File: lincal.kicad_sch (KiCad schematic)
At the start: 0 parts

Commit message: Most blocks there....
About to restore scan.
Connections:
- no-connect marks 2 -> 6
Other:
- sheet DAC2752-1A ports: added none; removed Comp
- sheet DAC2752-1B ports: added none; removed Comp
- sheet DAC2752-2A ports: added none; removed Comp
- sheet DAC2752-2B ports: added none; removed Comp
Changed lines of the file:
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@@
 	(paper "A4")
 	(no_connect
+		(at 195.58 110.49)
+	)
+	(no_connect
+		(at 195.58 120.65)
+	)
+	(no_connect
 		(at 195.58 118.11)
+	)
+	(no_connect
+		(at 195.58 107.95)
+	)
+	(no_connect
+		(at 195.58 113.03)
 	)
 	(no_connect
@@
 	(wire
 		(pts
+			(xy 194.31 120.65) (xy 195.58 120.65)
+		)
+		(stroke
+			(width 0)
+			(type default)
+		)
+	)
+	(wire
+		(pts
 			(xy 48.26 142.24) (xy 58.42 142.24)
 		)
@@
 	(wire
 		(pts
+			(xy 194.31 113.03) (xy 195.58 113.03)
+		)
+		(stroke
+			(width 0)
+			(type default)
+		)
+	)
+	(wire
+		(pts
 			(xy 58.42 146.05) (xy 48.26 146.05)
 		)
@@
 	(wire
 		(pts
+			(xy 194.31 110.49) (xy 195.58 110.49)
+		)
+		(stroke
+			(width 0)
+			(type default)
+		)
+	)
+	(wire
+		(pts
 			(xy 176.53 102.87) (xy 167.64 102.87)
 		)
@@
 	(wire
 		(pts
-			(xy 194.31 110.49) (xy 204.47 110.49)
-		)
-		(stroke
-			(width 0)
-			(type default)
-		)
-	)
-	(wire
-		(pts
-			(xy 194.31 113.03) (xy 204.47 113.03)
+			(xy 194.31 102.87) (xy 204.47 102.87)
 		)
 		(stroke
@@
 	(wire
 		(pts
-			(xy 194.31 107.95) (xy 204.47 107.95)
-		)
-		(stroke
-			(width 0)
-			(type default)
-		)
-	)
-	(wire
-		(pts
 			(xy 81.28 148.59) (xy 90.17 148.59)
 		)
@@
 	(wire
 		(pts
-			(xy 194.31 120.65) (xy 204.47 120.65)
+			(xy 194.31 105.41) (xy 204.47 105.41)
 		)
 		(stroke
@@
 	(wire
 		(pts
-			(xy 58.42 78.74) (xy 48.26 78.74)
-		)
-		(stroke
-			(width 0)
-			(type default)
-		)
-	)
-	(wire
-		(pts
 			(xy 140.97 57.15) (xy 148.59 57.15)
 		)
@@
 	(wire
 		(pts
-			(xy 58.42 116.84) (xy 48.26 116.84)
-		)
-		(stroke
-			(width 0)
-			(type default)
-		)
-	)
-	(wire
-		(pts
 			(xy 198.12 77.47) (xy 207.01 77.47)
 		)
@@
 	(wire
 		(pts
-			(xy 194.31 102.87) (xy 204.47 102.87)
-		)
-		(stroke
-			(width 0)
-			(type default)
-		)
-	)
-	(wire
-		(pts
 			(xy 198.12 59.69) (xy 207.01 59.69)
 		)
@@
 	(wire
 		(pts
-			(xy 58.42 104.14) (xy 48.26 104.14)
-		)
-		(stroke
-			(width 0)
-			(type default)
-		)
-	)
-	(wire
-		(pts
-			(xy 58.42 91.44) (xy 48.26 91.44)
+			(xy 194.31 107.95) (xy 195.58 107.95)
 		)
 		(stroke
@@
 		(pts
 			(xy 114.3 57.15) (xy 105.41 57.15)
-		)
-		(stroke
-			(width 0)
-			(type default)
-		)
-	)
-	(wire
-		(pts
-			(xy 194.31 105.41) (xy 204.47 105.41)
 		)
 		(stroke
@@
 		)
 	)
-	(label "Comp2A"
-		(at 48.26 104.14 0)
-		(effects
-			(font
-				(size 1.27 1.27)
-			)
-			(justify left bottom)
-		)
-	)
 	(label "MonB1"
 		(at 90.17 148.59 180)
@@
 		)
 	)
-	(label "Comp2A"
-		(at 204.47 107.95 180)
-		(effects
-			(font
-				(size 1.27 1.27)
-			)
-			(justify right bottom)
-		)
-	)
 	(label "~{CSDAC1}"
 		(at 90.17 57.15 180)
@@
 	)
 	(label "MonTC"
-		(at 204.47 113.03 180)
+		(at 204.47 102.87 180)
 		(effects
 			(font
@@
 	)
 	(label "Ref2V16"
-		(at 204.47 120.65 180)
-		(effects
-			(font
-				(size 1.27 1.27)
-			)
-			(justify right bottom)
-		)
-	)
-	(label "Comp2B"
-		(at 48.26 116.84 0)
-		(effects
-			(font
-				(size 1.27 1.27)
-			)
-			(justify left bottom)
-		)
-	)
-	(label "Comp1A"
-		(at 48.26 78.74 0)
-		(effects
-			(font
-				(size 1.27 1.27)
-			)
-			(justify left bottom)
+		(at 204.47 105.41 180)
+		(effects
+			(font
+				(size 1.27 1.27)
+			)
+			(justify right bottom)
 		)
 	)
@@
 		)
 	)
-	(label "Comp2B"
-		(at 204.47 110.49 180)
-		(effects
-			(font
-				(size 1.27 1.27)
-			)
-			(justify right bottom)
-		)
-	)
 	(label "OffsetA2"
 		(at 207.01 62.23 180)
@@
 		)
 	)
-	(label "Comp1B"
-		(at 48.26 91.44 0)
-		(effects
-			(font
-				(size 1.27 1.27)
-			)
-			(justify left bottom)
-		)
-	)
 	(label "Sel1A"
 		(at 162.56 72.39 0)
@@
 		)
 	)
-	(label "Comp1B"
-		(at 204.47 105.41 180)
-		(effects
-			(font
-				(size 1.27 1.27)
-			)
-			(justify right bottom)
-		)
-	)
 	(label "MOSI"
 		(at 49.53 57.15 0)
@@
 			)
 			(justify left bottom)
-		)
-	)
-	(label "Comp1A"
-		(at 204.47 102.87 180)
-		(effects
-			(font
-				(size 1.27 1.27)
-			)
-			(justify right bottom)
 		)
 	)
@@
 			)
 		)
-		(pin "Comp" input
-			(at 58.42 91.44 180)
-			(effects
-				(font
-					(size 1.27 1.27)
-				)
-				(justify left)
-			)
-		)
 		(pin "Select" input
 			(at 81.28 90.17 0)
@@
 			)
 		)
-		(pin "Comp" input
-			(at 58.42 104.14 180)
-			(effects
-				(font
-					(size 1.27 1.27)
-				)
-				(justify left)
-			)
-		)
 		(pin "Select" input
 			(at 81.28 102.87 0)
@@
 			)
 		)
-		(pin "Comp" input
-			(at 58.42 116.84 180)
-			(effects
-				(font
-					(size 1.27 1.27)
-				)
-				(justify left)
-			)
-		)
 		(pin "Select" input
 			(at 81.28 115.57 0)
@@
 			(effects
 				(font
-					(size 1.27 1.27)
-				)
-				(justify left)
-			)
-		)
-		(pin "Comp" input
-			(at 58.42 78.74 180)
-			(effects
-				(font

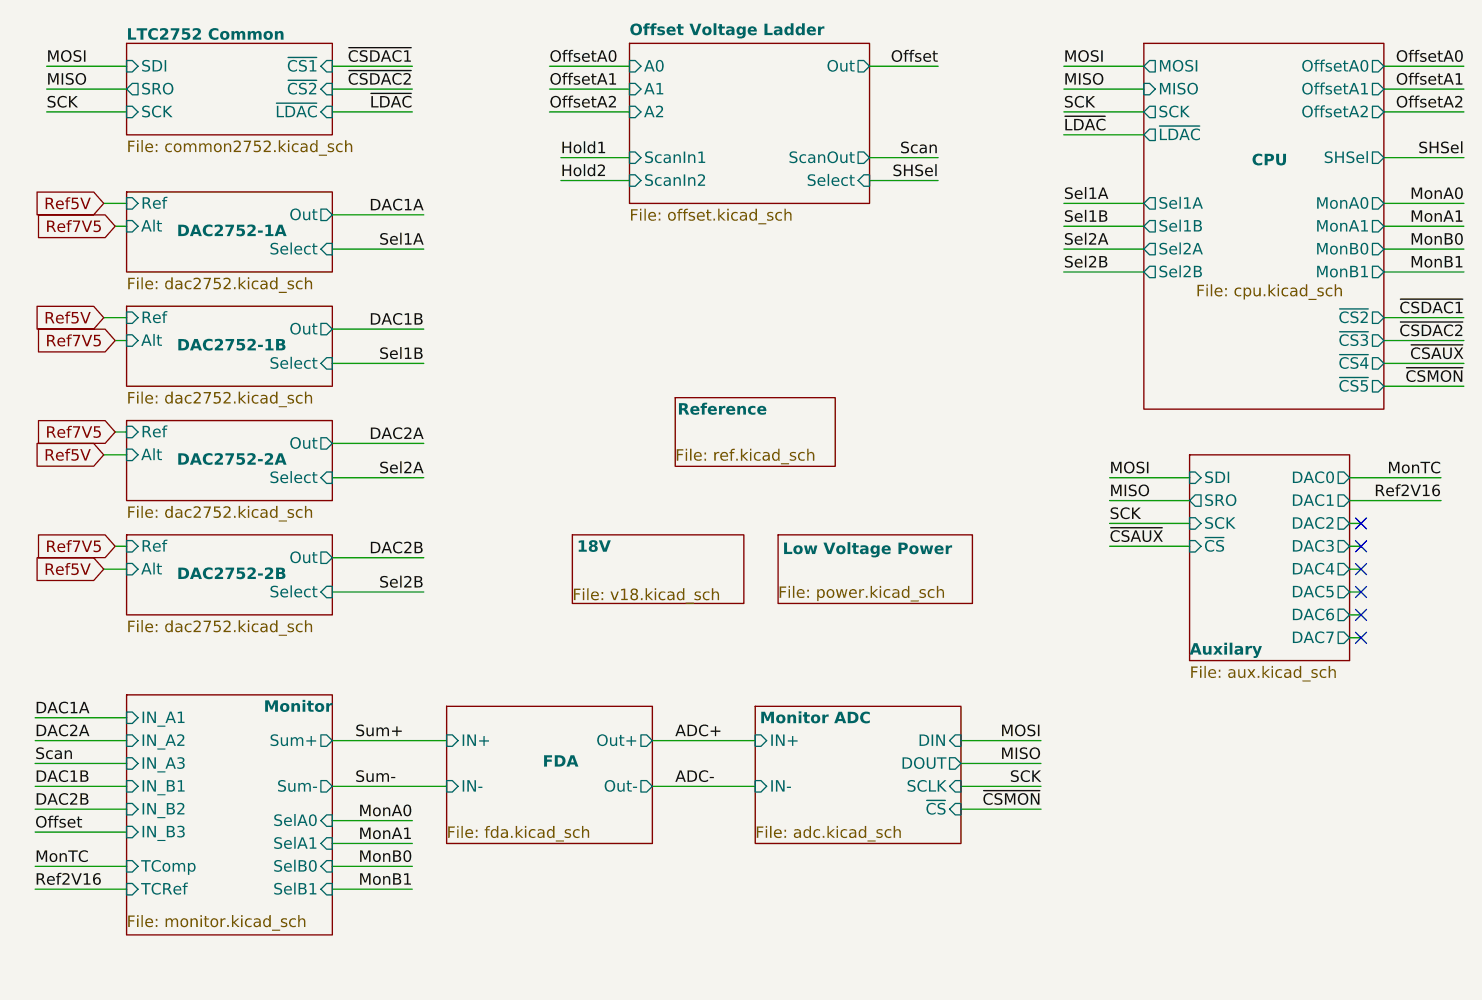
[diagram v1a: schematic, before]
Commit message: S&H restored.  Now to touch up connections etc.
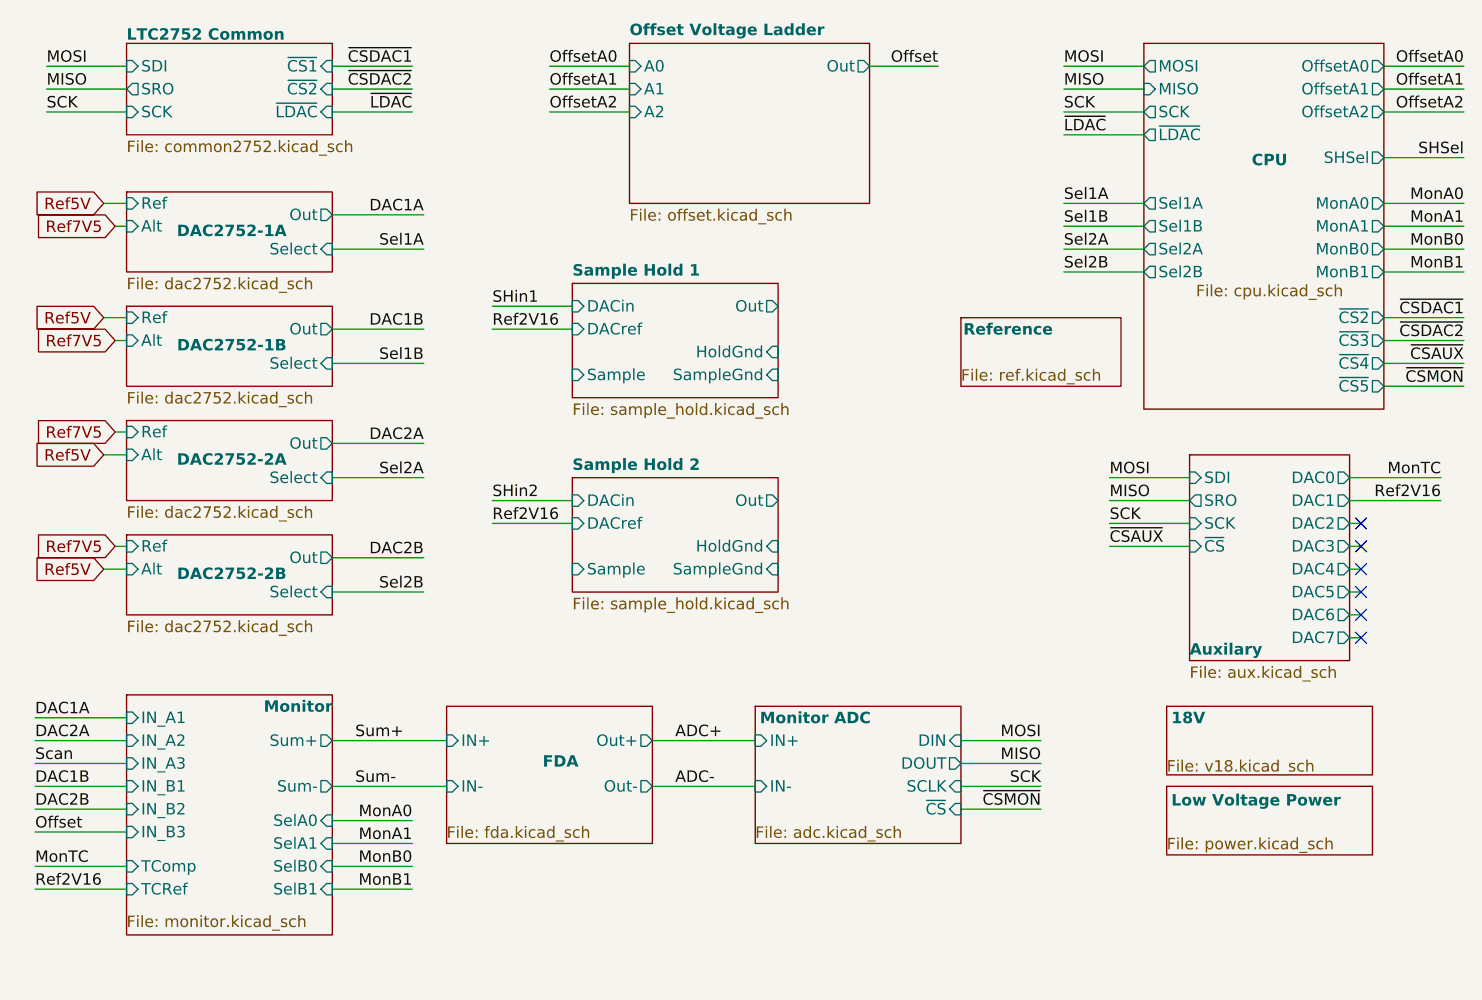
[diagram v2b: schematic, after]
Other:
- added sheet Sample Hold 1 (sample_hold.kicad_sch)
- added sheet Sample Hold 2 (sample_hold.kicad_sch)
- sheet Offset Voltage Ladder ports: added none; removed ScanIn1, ScanIn2, ScanOut, Select

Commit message: Put ref filtering into the schematic.
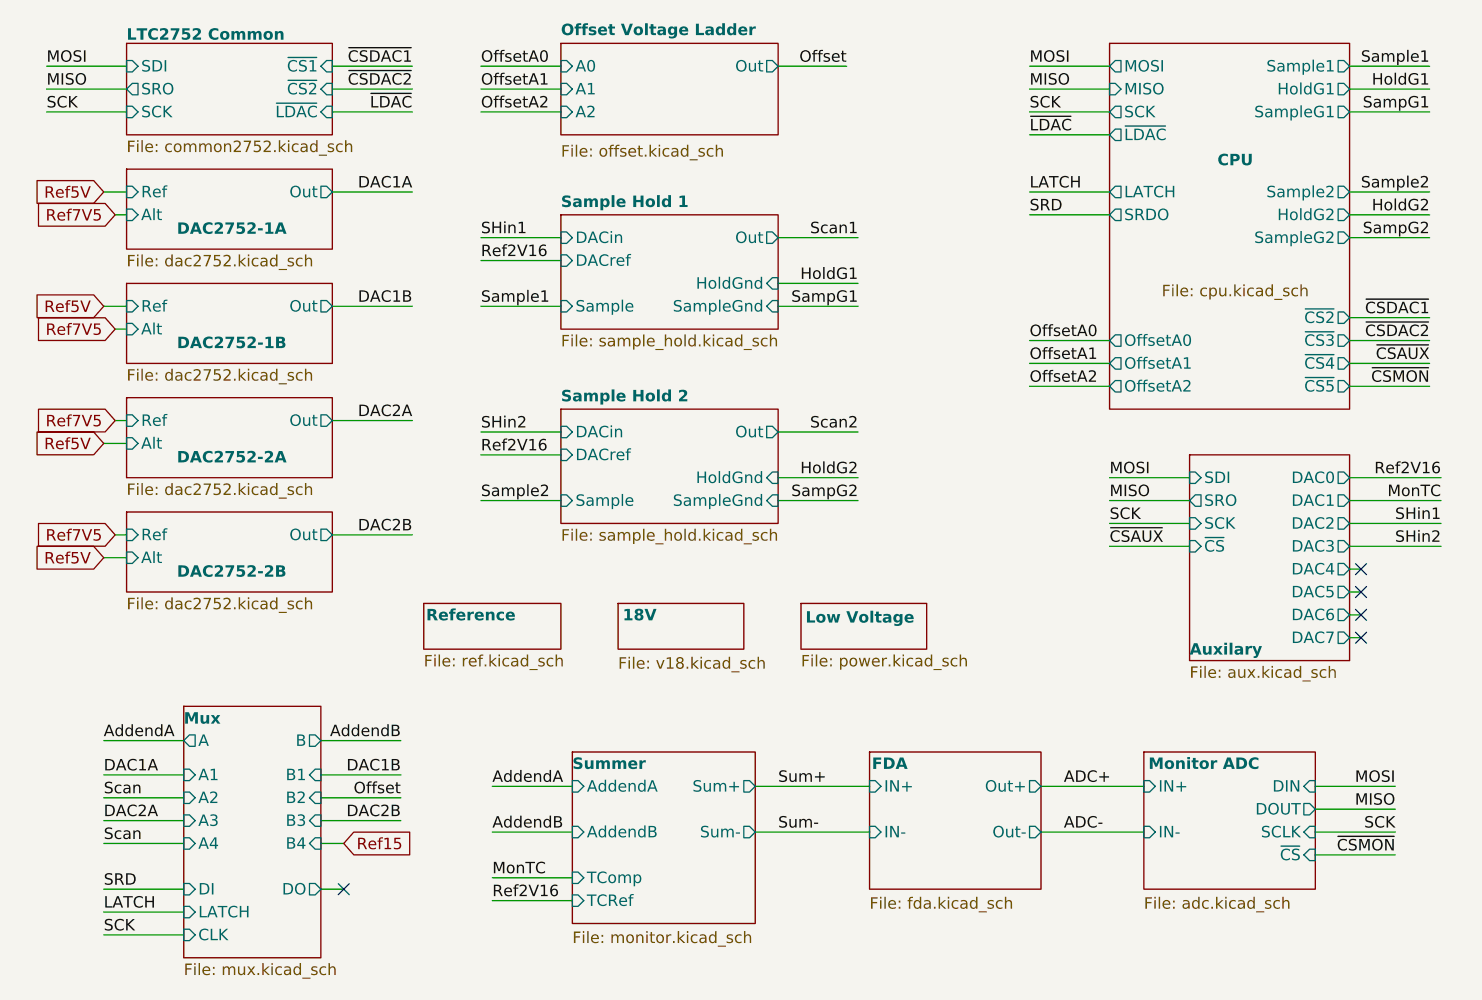
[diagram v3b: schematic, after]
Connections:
- no-connect marks 6 -> 5
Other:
- sheet Low Voltage Power renamed Low Voltage
- sheet Monitor renamed Summer
- added sheet Mux (mux.kicad_sch)
- sheet CPU ports: added HoldG1, HoldG2, LATCH, SRDO, Sample1, Sample2, SampleG1, SampleG2; removed MonA0, MonA1, MonB0, MonB1, SHSel, Sel1A, Sel1B, Sel2A, Sel2B
- sheet DAC2752-1A ports: added none; removed Select
- sheet DAC2752-1B ports: added none; removed Select
- sheet DAC2752-2A ports: added none; removed Select
- sheet DAC2752-2B ports: added none; removed Select
- sheet Summer ports: added AddendA, AddendB; removed IN_A1, IN_A2, IN_A3, IN_B1, IN_B2, IN_B3, SelA0, SelA1, SelB0, SelB1

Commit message: Adjust voltage rails.
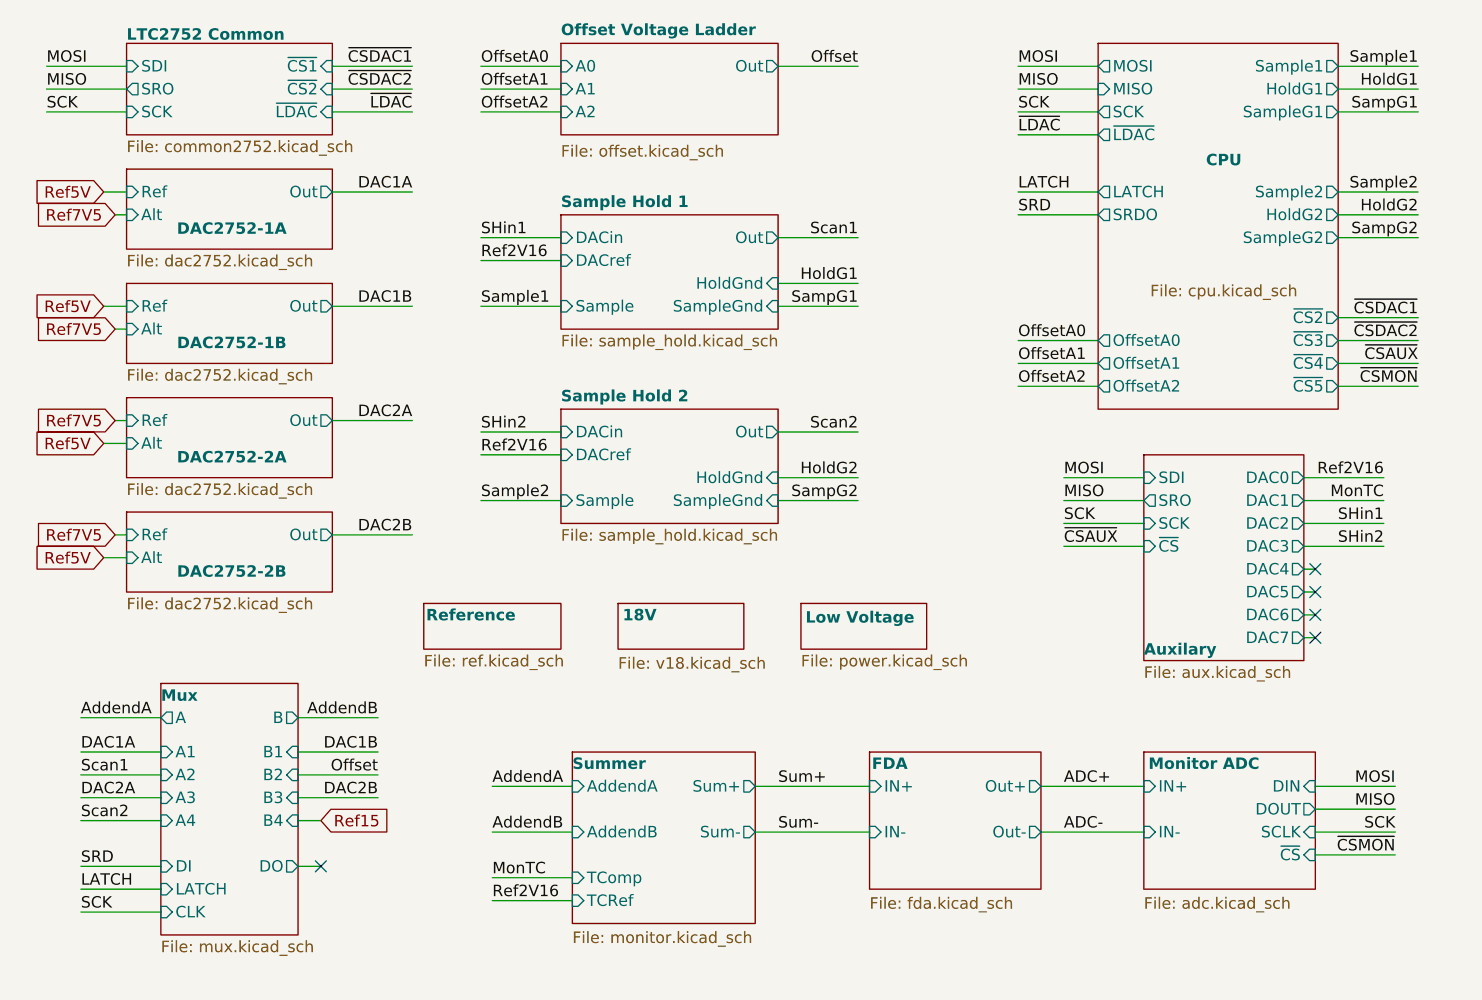
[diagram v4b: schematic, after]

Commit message: Progress checkin.  About to redo FDA feedback again.
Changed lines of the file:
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@@
 		)
 	)
-	(global_label "Ref15"
+	(global_label "Ref10V"
 		(shape input)
 		(at 80.01 140.97 0)
@@
 		)
 		(property "Intersheetrefs" "${INTERSHEET_REFS}"
-			(at 86.4665 140.97 0)
+			(at 87.7365 140.97 0)
 			(effects
 				(font

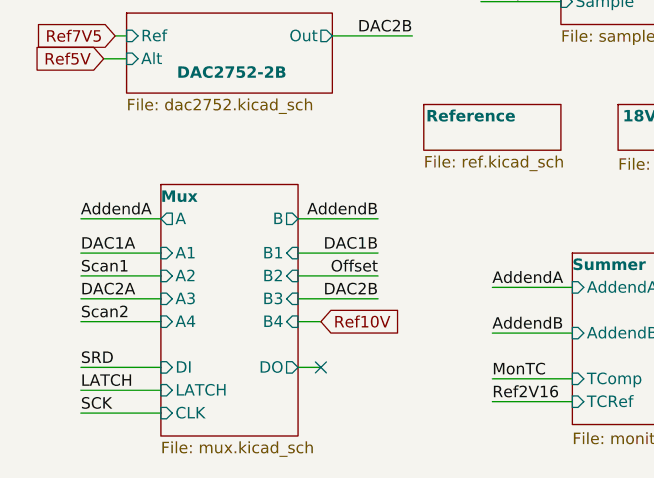
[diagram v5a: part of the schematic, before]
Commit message: Power mostly routed
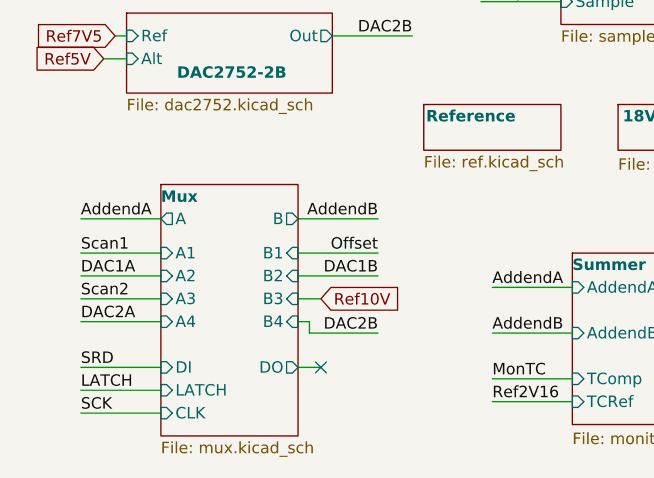
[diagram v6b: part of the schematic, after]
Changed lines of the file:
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@@
+	(wire
+		(pts
+			(xy 78.74 142.24) (xy 78.74 140.97)
+		)
+		(stroke
+			(width 0)
+			(type default)
+		)
+	)
 	(wire
 		(pts
@@
 	(wire
 		(pts
-			(xy 77.47 138.43) (xy 86.36 138.43)
+			(xy 78.74 142.24) (xy 86.36 142.24)
 		)
 		(stroke
@@
 	(wire
 		(pts
-			(xy 77.47 140.97) (xy 80.01 140.97)
+			(xy 77.47 138.43) (xy 80.01 138.43)
 		)
 		(stroke
@@
 		(pts
 			(xy 97.79 83.82) (xy 106.68 83.82)
+		)
+		(stroke
+			(width 0)
+			(type default)
+		)
+	)
+	(wire
+		(pts
+			(xy 78.74 140.97) (xy 77.47 140.97)
 		)
 		(stroke
@@
 	)
 	(label "Scan1"
-		(at 53.34 135.89 0)
+		(at 53.34 133.35 0)
 		(effects
 			(font
@@
 	)
 	(label "DAC2A"
-		(at 53.34 138.43 0)
+		(at 53.34 140.97 0)
 		(effects
 			(font
@@
 	)
 	(label "DAC1B"
-		(at 86.36 133.35 180)
+		(at 86.36 135.89 180)
 		(effects
 			(font
@@
 	)
 	(label "Offset"
-		(at 86.36 135.89 180)
+		(at 86.36 133.35 180)
 		(effects
 			(font
@@
 	)
 	(label "DAC2B"
-		(at 86.36 138.43 180)
+		(at 86.36 142.24 180)
 		(effects
 			(font
@@
 	)
 	(label "Scan2"
-		(at 53.34 140.97 0)
+		(at 53.34 138.43 0)
 		(effects
 			(font
@@
 	)
 	(label "DAC1A"
-		(at 53.34 133.35 0)
+		(at 53.34 135.89 0)
 		(effects
 			(font
@@
 	(global_label "Ref10V"
 		(shape input)
-		(at 80.01 140.97 0)
+		(at 80.01 138.43 0)
 		(effects
 			(font
@@
 		)
 		(property "Intersheetrefs" "${INTERSHEET_REFS}"
-			(at 87.7365 140.97 0)
+			(at 87.7365 138.43 0)
 			(effects
 				(font
